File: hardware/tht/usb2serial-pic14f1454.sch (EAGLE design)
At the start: 14 parts, among them IC1 PIC16F1454, IC2 LP2950-33, J1 USB-SHIELD-A-H, J2 J2

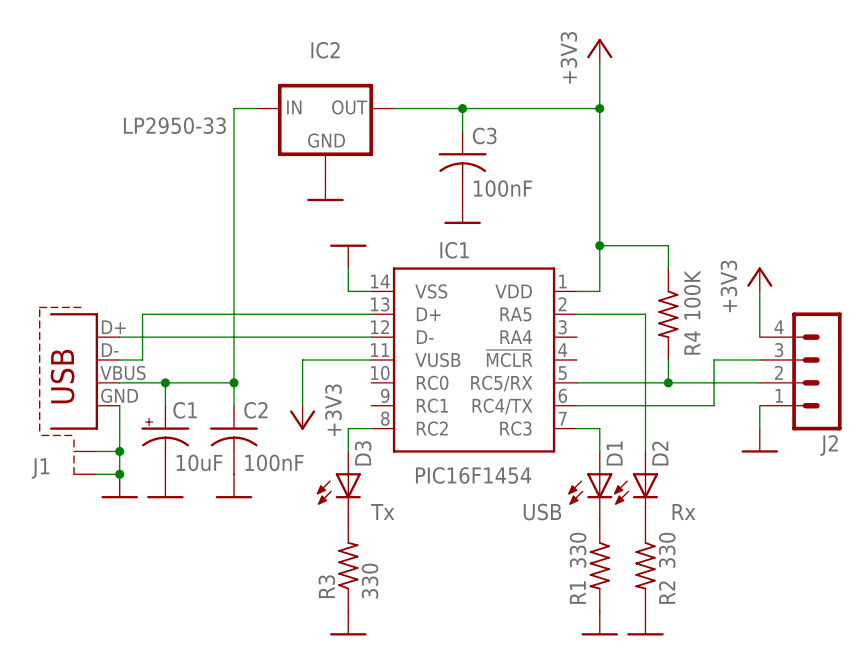
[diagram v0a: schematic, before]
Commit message: Fixed D+/D- bug
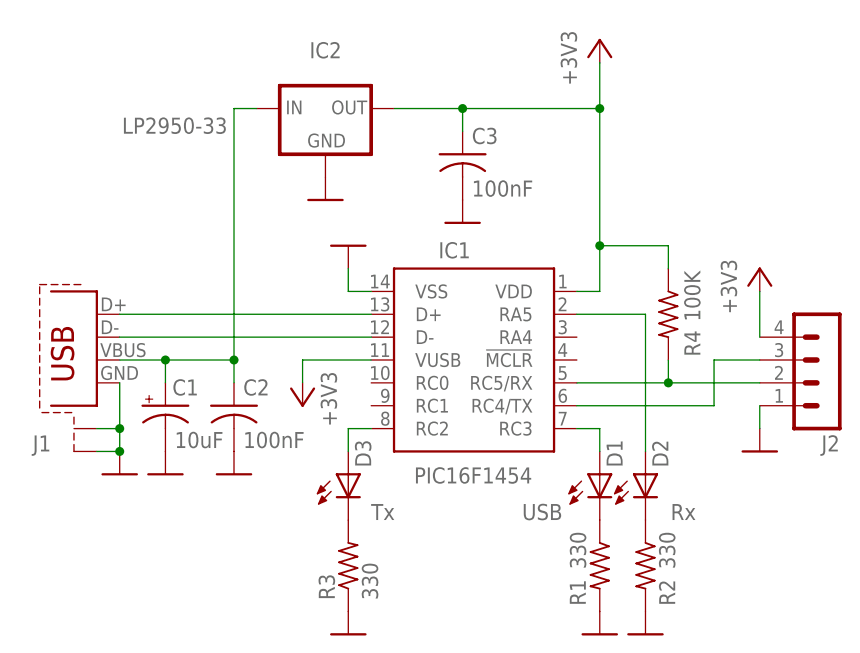
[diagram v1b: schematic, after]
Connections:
- net N$1: now also IC1.D-; no longer IC1.D+
- net N$2: now also IC1.D+; no longer IC1.D-
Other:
- moved on the sheet: C1, C2, J1
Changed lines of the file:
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@@
 </plain>
 <instances>
-<instance part="GND15" gate="1" x="15.24" y="25.4" smashed="yes"/>
-<instance part="J1" gate="G$1" x="12.7" y="38.1" smashed="yes" rot="MR0">
-<attribute name="NAME" x="7.62" y="27.94" size="1.778" layer="95" rot="MR0"/>
-</instance>
-<instance part="GND1" gate="1" x="20.32" y="25.4" smashed="yes"/>
+<instance part="GND15" gate="1" x="15.24" y="27.94" smashed="yes"/>
+<instance part="J1" gate="G$1" x="12.7" y="40.64" smashed="yes" rot="MR0">
+<attribute name="NAME" x="7.62" y="30.48" size="1.778" layer="95" rot="MR0"/>
+</instance>
+<instance part="GND1" gate="1" x="20.32" y="27.94" smashed="yes"/>
 <instance part="J2" gate="1" x="93.98" y="40.64" smashed="yes" rot="MR0">
 <attribute name="VALUE" x="95.25" y="30.48" size="1.778" layer="96" rot="MR0"/>
@@
 <attribute name="VALUE" x="54.356" y="58.801" size="1.778" layer="96"/>
 </instance>
-<instance part="C1" gate="G$1" x="20.32" y="33.02" smashed="yes">
-<attribute name="NAME" x="21.082" y="34.163" size="1.778" layer="95"/>
-<attribute name="VALUE" x="21.336" y="28.321" size="1.778" layer="96"/>
-</instance>
-<instance part="+3V4" gate="G$1" x="35.56" y="33.02" rot="R180"/>
+<instance part="C1" gate="G$1" x="20.32" y="35.56" smashed="yes">
+<attribute name="NAME" x="21.082" y="36.703" size="1.778" layer="95"/>
+<attribute name="VALUE" x="21.336" y="30.861" size="1.778" layer="96"/>
+</instance>
+<instance part="+3V4" gate="G$1" x="35.56" y="35.56" smashed="yes" rot="R180">
+<attribute name="VALUE" x="37.592" y="39.37" size="1.778" layer="96" rot="R270"/>
+</instance>
 <instance part="+3V1" gate="G$1" x="86.36" y="50.8"/>
 <instance part="+3V3" gate="G$1" x="68.58" y="76.2"/>
@@
 </instance>
 <instance part="GND9" gate="1" x="53.34" y="55.88" smashed="yes"/>
-<instance part="C2" gate="G$1" x="27.94" y="33.02" smashed="yes">
-<attribute name="NAME" x="28.956" y="34.163" size="1.778" layer="95"/>
-<attribute name="VALUE" x="28.956" y="28.321" size="1.778" layer="96"/>
-</instance>
-<instance part="GND10" gate="1" x="27.94" y="25.4" smashed="yes"/>
+<instance part="C2" gate="G$1" x="27.94" y="35.56" smashed="yes">
+<attribute name="NAME" x="28.956" y="36.703" size="1.778" layer="95"/>
+<attribute name="VALUE" x="28.956" y="30.861" size="1.778" layer="96"/>
+</instance>
+<instance part="GND10" gate="1" x="27.94" y="27.94" smashed="yes"/>
 </instances>
 <busses>
@@
 <segment>
 <pinref part="J1" gate="G$1" pin="GND"/>
-<wire x1="15.24" y1="35.56" x2="15.24" y2="30.48" width="0.1524" layer="91"/>
+<wire x1="15.24" y1="38.1" x2="15.24" y2="33.02" width="0.1524" layer="91"/>
 <pinref part="GND15" gate="1" pin="GND"/>
 <pinref part="J1" gate="G$1" pin="S1"/>
-<wire x1="15.24" y1="30.48" x2="15.24" y2="27.94" width="0.1524" layer="91"/>
+<wire x1="15.24" y1="33.02" x2="15.24" y2="30.48" width="0.1524" layer="91"/>
+<wire x1="12.7" y1="33.02" x2="15.24" y2="33.02" width="0.1524" layer="91"/>
+<junction x="15.24" y="33.02"/>
+<pinref part="J1" gate="G$1" pin="S2"/>
 <wire x1="12.7" y1="30.48" x2="15.24" y2="30.48" width="0.1524" layer="91"/>
 <junction x="15.24" y="30.48"/>
-<pinref part="J1" gate="G$1" pin="S2"/>
-<wire x1="12.7" y1="27.94" x2="15.24" y2="27.94" width="0.1524" layer="91"/>
-<junction x="15.24" y="27.94"/>
 </segment>
 <segment>
@@
 <segment>
 <pinref part="J1" gate="G$1" pin="D-"/>
-<wire x1="15.24" y1="40.64" x2="17.78" y2="40.64" width="0.1524" layer="91"/>
-<wire x1="17.78" y1="40.64" x2="17.78" y2="45.72" width="0.1524" layer="91"/>
+<wire x1="15.24" y1="43.18" x2="43.18" y2="43.18" width="0.1524" layer="91"/>
+<pinref part="IC1" gate="G$1" pin="D-"/>
+</segment>
+</net>
+<net name="N$2" class="0">
+<segment>
+<pinref part="J1" gate="G$1" pin="D+"/>
+<wire x1="15.24" y1="45.72" x2="43.18" y2="45.72" width="0.1524" layer="91"/>
 <pinref part="IC1" gate="G$1" pin="D+"/>
-<wire x1="17.78" y1="45.72" x2="43.18" y2="45.72" width="0.1524" layer="91"/>
-</segment>
-</net>
-<net name="N$2" class="0">
-<segment>
-<wire x1="43.18" y1="43.18" x2="15.24" y2="43.18" width="0.1524" layer="91"/>
-<pinref part="J1" gate="G$1" pin="D+"/>
-<pinref part="IC1" gate="G$1" pin="D-"/>
 </segment>
 </net>
@@
 <pinref part="IC1" gate="G$1" pin="VUSB"/>
 <wire x1="43.18" y1="40.64" x2="35.56" y2="40.64" width="0.1524" layer="91"/>
-<wire x1="35.56" y1="40.64" x2="35.56" y2="35.56" width="0.1524" layer="91"/>
+<wire x1="35.56" y1="40.64" x2="35.56" y2="38.1" width="0.1524" layer="91"/>
 <pinref part="+3V4" gate="G$1" pin="+3V3"/>
 </segment>
@@
 <segment>
 <pinref part="J1" gate="G$1" pin="VBUS"/>
-<wire x1="15.24" y1="38.1" x2="20.32" y2="38.1" width="0.1524" layer="91"/>
-<wire x1="20.32" y1="38.1" x2="20.32" y2="35.56" width="0.1524" layer="91"/>
-<junction x="20.32" y="38.1"/>
+<wire x1="15.24" y1="40.64" x2="20.32" y2="40.64" width="0.1524" layer="91"/>
+<wire x1="20.32" y1="40.64" x2="20.32" y2="38.1" width="0.1524" layer="91"/>
+<junction x="20.32" y="40.64"/>
 <pinref part="C1" gate="G$1" pin="+"/>
 <pinref part="IC2" gate="1" pin="IN"/>
-<wire x1="20.32" y1="38.1" x2="27.94" y2="38.1" width="0.1524" layer="91"/>
+<wire x1="20.32" y1="40.64" x2="27.94" y2="40.64" width="0.1524" layer="91"/>
 <pinref part="C2" gate="G$1" pin="1"/>
-<wire x1="27.94" y1="38.1" x2="27.94" y2="35.56" width="0.1524" layer="91"/>
-<wire x1="27.94" y1="38.1" x2="27.94" y2="68.58" width="0.1524" layer="91"/>
-<junction x="27.94" y="38.1"/>
+<wire x1="27.94" y1="40.64" x2="27.94" y2="38.1" width="0.1524" layer="91"/>
+<wire x1="27.94" y1="40.64" x2="27.94" y2="68.58" width="0.1524" layer="91"/>
+<junction x="27.94" y="40.64"/>
 <wire x1="27.94" y1="68.58" x2="30.48" y2="68.58" width="0.1524" layer="91"/>
 </segment>
